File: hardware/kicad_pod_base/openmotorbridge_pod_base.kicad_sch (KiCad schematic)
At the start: 4 parts, among them J1 MILL_MAX_824_POGO_6P, J2 M8_6PIN_RECEPTACLE, U1 SP3012-06UTG

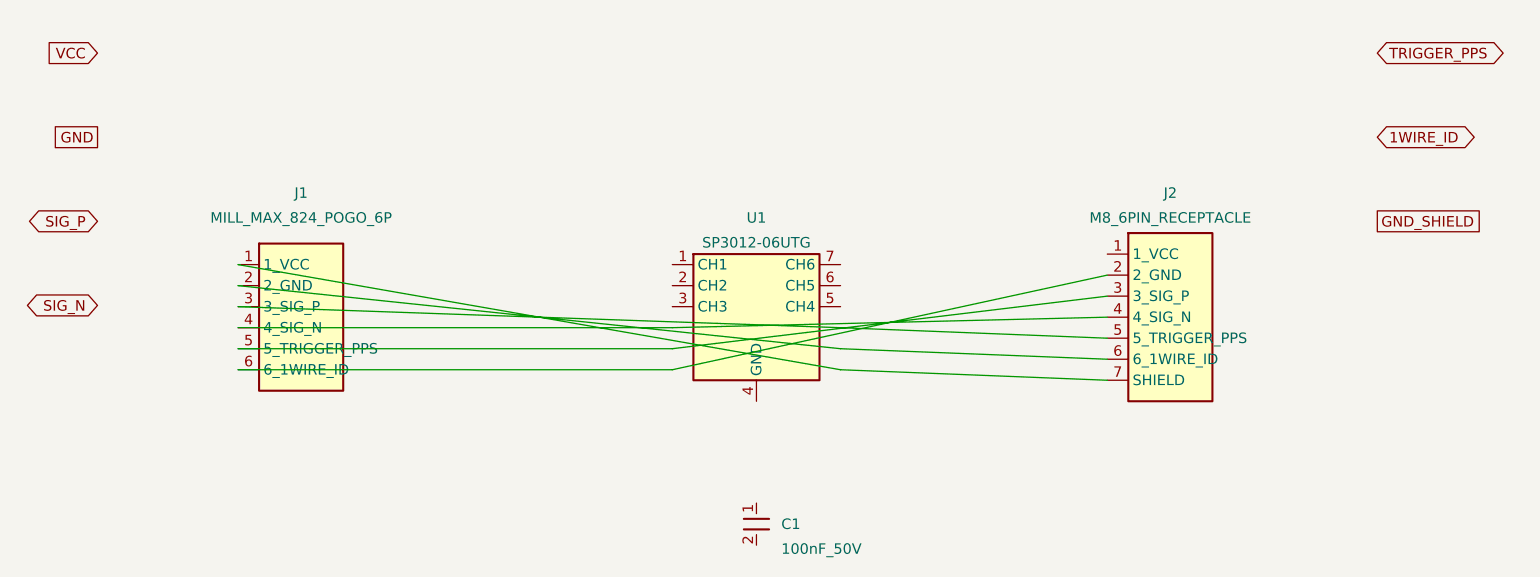
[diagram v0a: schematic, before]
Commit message: feat(hardware): implement dual-port pod base, magsafe frame dock, and saddlebag split grommet
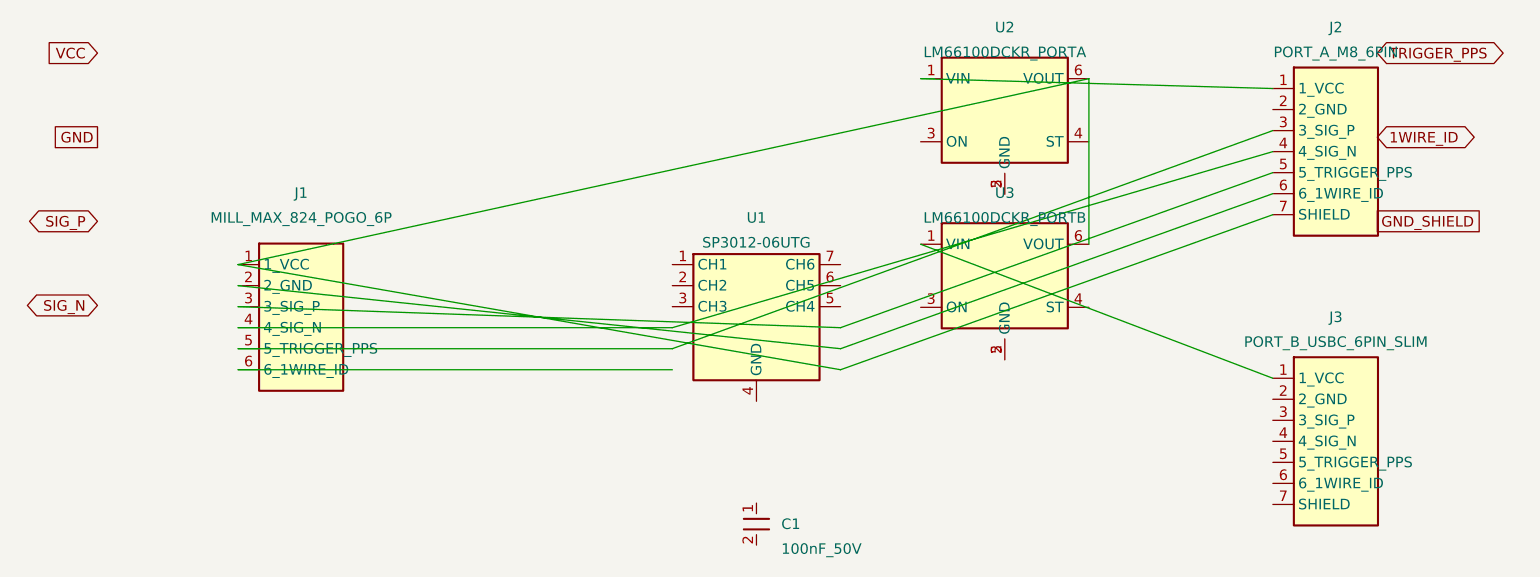
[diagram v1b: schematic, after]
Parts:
- added J3: PORT_B_USBC_6PIN_SLIM, Connector_USB:USB_C_Receptacle_HRO_TYPE-C-31-M-12, symbol Connector:Conn_01x07_Shield
- added U2: LM66100DCKR_PORTA, Package_TO_SOT_SMD:SOT-363_SC-70-6, symbol Power_Management:LM66100DCKR
- added U3: LM66100DCKR_PORTB, Package_TO_SOT_SMD:SOT-363_SC-70-6, symbol Power_Management:LM66100DCKR
- J1: footprint Connector_PinHeader_2.54mm:PinHeader_1x06_P2.54mm_Vertical -> Connector_PinHeader_2.54mm:PinHeader_1x06_P2.54mm_Vertical_SMD_Pin1Left
- J2: value M8_6PIN_RECEPTACLE -> PORT_A_M8_6PIN; footprint Connector_PinHeader_2.54mm:PinHeader_1x07_P2.54mm_Vertical -> Connector_M8:M8_6Pin_IP67_Receptacle_Socketed
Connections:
- net at J1.1 (1_VCC), J2.7 (SHIELD): now also U2.6 (VOUT), U3.6 (VOUT)
- net at J1.6 (6_1WIRE_ID): no longer J2.2 (2_GND)
- net at J2.1 (1_VCC): now also U2.1 (VIN)
- new net: U2.2 (GND), U2.5 (GND)
- new net: J3.1 (1_VCC), U3.1 (VIN)
- new net: U3.2 (GND), U3.5 (GND)
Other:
- title: OpenMotorBridge v8.0 - Pod-Bodenplatine (Pod-Base PCB) -> OpenMotorBridge v8.1 - Dual-Port Pod-Bodenplatine (Pod-Base PCB)
- moved on the sheet: J2
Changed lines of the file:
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@@
 	(paper "A4")
 	(title_block
-		(title "OpenMotorBridge v8.0 - Pod-Bodenplatine (Pod-Base PCB)")
-		(date "2026-08-24")
-		(rev "v8.0")
+		(title "OpenMotorBridge v8.1 - Dual-Port Pod-Bodenplatine (Pod-Base PCB)")
+		(date "2026-09-06")
+		(rev "v8.1")
 		(company "OpenMotorBridge Open Source Hardware")
-		(comment 1 "Mill-Max 6-Pin Pogo-Pin Array + Littelfuse SP3012 ESD-Array + M8 Einbaubuchse")
-		(comment 2 "Versiegelter Übergang vom Kassettenboden zum M8-Kabelbaum")
+		(comment 1 "Dual-Port: Port A (M8 6P IP67) + Port B (USB-C 6P Slim) mit TI LM66100 Ideal-Diode Power-Mux")
+		(comment 2 "Mill-Max 6P Pogo J1 mittig zentriert, Littelfuse SP3012 ESD-Array, 36x20mm Monocoque-Fit")
 	)
 	(global_label "VCC" (shape input) (at 25.4 38.1 180) (effects (font (size 1.27 1.27)) (justify right)))
@@
 		(property "Reference" "J1" (at 50.0 55.0 0) (effects (font (size 1.27 1.27))))
 		(property "Value" "MILL_MAX_824_POGO_6P" (at 50.0 58.0 0) (effects (font (size 1.27 1.27))))
-		(property "Footprint" "Connector_PinHeader_2.54mm:PinHeader_1x06_P2.54mm_Vertical" (at 0 0 0) (effects (font (size 1.27 1.27)) hide))
+		(property "Footprint" "Connector_PinHeader_2.54mm:PinHeader_1x06_P2.54mm_Vertical_SMD_Pin1Left" (at 0 0 0) (effects (font (size 1.27 1.27)) hide))
 		(property "LCSC" "C224376" (at 0 0 0) (effects (font (size 1.27 1.27)) hide))
 		(pin "1")
@@
 		(pin "2")
 	)
-	(symbol (lib_id "Connector:Conn_01x07_Shield") (at 155.0 70.0 0) (unit 1)
+	(symbol (lib_id "Power_Management:LM66100DCKR") (at 135.0 45.0 0) (unit 1)
 		(in_bom yes) (on_board yes) (dnp no)
-		(property "Reference" "J2" (at 155.0 55.0 0) (effects (font (size 1.27 1.27))))
-		(property "Value" "M8_6PIN_RECEPTACLE" (at 155.0 58.0 0) (effects (font (size 1.27 1.27))))
-		(property "Footprint" "Connector_PinHeader_2.54mm:PinHeader_1x07_P2.54mm_Vertical" (at 0 0 0) (effects (font (size 1.27 1.27)) hide))
+		(property "Reference" "U2" (at 135.0 35.0 0) (effects (font (size 1.27 1.27))))
+		(property "Value" "LM66100DCKR_PORTA" (at 135.0 38.0 0) (effects (font (size 1.27 1.27))))
+		(property "Footprint" "Package_TO_SOT_SMD:SOT-363_SC-70-6" (at 0 0 0) (effects (font (size 1.27 1.27)) hide))
+		(property "LCSC" "C2913168" (at 0 0 0) (effects (font (size 1.27 1.27)) hide))
+		(pin "1")
+		(pin "2")
+		(pin "3")
+		(pin "4")
+		(pin "5")
+		(pin "6")
+	)
+	(symbol (lib_id "Power_Management:LM66100DCKR") (at 135.0 65.0 0) (unit 1)
+		(in_bom yes) (on_board yes) (dnp no)
+		(property "Reference" "U3" (at 135.0 55.0 0) (effects (font (size 1.27 1.27))))
+		(property "Value" "LM66100DCKR_PORTB" (at 135.0 58.0 0) (effects (font (size 1.27 1.27))))
+		(property "Footprint" "Package_TO_SOT_SMD:SOT-363_SC-70-6" (at 0 0 0) (effects (font (size 1.27 1.27)) hide))
+		(property "LCSC" "C2913168" (at 0 0 0) (effects (font (size 1.27 1.27)) hide))
+		(pin "1")
+		(pin "2")
+		(pin "3")
+		(pin "4")
+		(pin "5")
+		(pin "6")
+	)
+	(symbol (lib_id "Connector:Conn_01x07_Shield") (at 175.0 50.0 0) (unit 1)
+		(in_bom yes) (on_board yes) (dnp no)
+		(property "Reference" "J2" (at 175.0 35.0 0) (effects (font (size 1.27 1.27))))
+		(property "Value" "PORT_A_M8_6PIN" (at 175.0 38.0 0) (effects (font (size 1.27 1.27))))
+		(property "Footprint" "Connector_M8:M8_6Pin_IP67_Receptacle_Socketed" (at 0 0 0) (effects (font (size 1.27 1.27)) hide))
 		(property "LCSC" "C2834590" (at 0 0 0) (effects (font (size 1.27 1.27)) hide))
+		(pin "1")
+		(pin "2")
+		(pin "3")
+		(pin "4")
+		(pin "5")
+		(pin "6")
+		(pin "7")
+	)
+	(symbol (lib_id "Connector:Conn_01x07_Shield") (at 175.0 85.0 0) (unit 1)
+		(in_bom yes) (on_board yes) (dnp no)
+		(property "Reference" "J3" (at 175.0 70.0 0) (effects (font (size 1.27 1.27))))
+		(property "Value" "PORT_B_USBC_6PIN_SLIM" (at 175.0 73.0 0) (effects (font (size 1.27 1.27))))
+		(property "Footprint" "Connector_USB:USB_C_Receptacle_HRO_TYPE-C-31-M-12" (at 0 0 0) (effects (font (size 1.27 1.27)) hide))
+		(property "LCSC" "C2765186" (at 0 0 0) (effects (font (size 1.27 1.27)) hide))
 		(pin "1")
 		(pin "2")
@@
 	(wire (pts (xy 42.38 66.19) (xy 115.16 73.81)) (stroke (width 0) (type solid)))
 	(wire (pts (xy 42.38 63.65) (xy 115.16 76.35)) (stroke (width 0) (type solid)))
-	(wire (pts (xy 115.16 76.35) (xy 147.38 77.62)) (stroke (width 0) (type solid)))
-	(wire (pts (xy 115.16 73.81) (xy 147.38 75.08)) (stroke (width 0) (type solid)))
-	(wire (pts (xy 115.16 71.27) (xy 147.38 72.54)) (stroke (width 0) (type solid)))
-	(wire (pts (xy 94.84 71.27) (xy 147.38 70.0)) (stroke (width 0) (type solid)))
-	(wire (pts (xy 94.84 73.81) (xy 147.38 67.46)) (stroke (width 0) (type solid)))
-	(wire (pts (xy 94.84 76.35) (xy 147.38 64.92)) (stroke (width 0) (type solid)))
+	(wire (pts (xy 115.16 76.35) (xy 167.38 57.62)) (stroke (width 0) (type solid)))
+	(wire (pts (xy 115.16 73.81) (xy 167.38 55.08)) (stroke (width 0) (type solid)))
+	(wire (pts (xy 115.16 71.27) (xy 167.38 52.54)) (stroke (width 0) (type solid)))
+	(wire (pts (xy 94.84 71.27) (xy 167.38 50.0)) (stroke (width 0) (type solid)))
+	(wire (pts (xy 94.84 73.81) (xy 167.38 47.46)) (stroke (width 0) (type solid)))
+	(wire (pts (xy 167.38 42.38) (xy 124.84 41.19)) (stroke (width 0) (type solid)))
+	(wire (pts (xy 167.38 77.38) (xy 124.84 61.19)) (stroke (width 0) (type solid)))
+	(wire (pts (xy 145.16 41.19) (xy 145.16 61.19)) (stroke (width 0) (type solid)))
+	(wire (pts (xy 145.16 41.19) (xy 42.38 63.65)) (stroke (width 0) (type solid)))
 )
